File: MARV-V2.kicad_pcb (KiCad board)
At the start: 4 copper layers, 46.6 x 41.2 mm, 140 parts, among them J10 DBG pads (SWCLK SWDIO GND), J11 microSD, Molex 104031-0811 pu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, J3 ESC pads (CURR TX M4 M3 M2 M1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, J4 USB_C_PROGRAM_POWER, J6 IO array signal column (inner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, J7 IO array power column (5V / 3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, J8 IO array GND column (board ed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, SW1 RESET (RUN to GND), SW2 BOOTSEL (via R24), U12 TPS7A2033PDBVR, U20 RP2354B, U21 ICM-45686 6-axis IMU, U22 BMP581 barometer, U23 ADXL375 high-g accelerometer, U24 DNP: W25Q32JVSNIQ, 32 Mbit QS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, U25 TPS2121RUXR, U26 AP63205WU-7, U7 TPS62913RPUR, U8 USBLC6-2SC6, Y1 12 MHz TAXM12M4RFBCCT2T, CL 1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

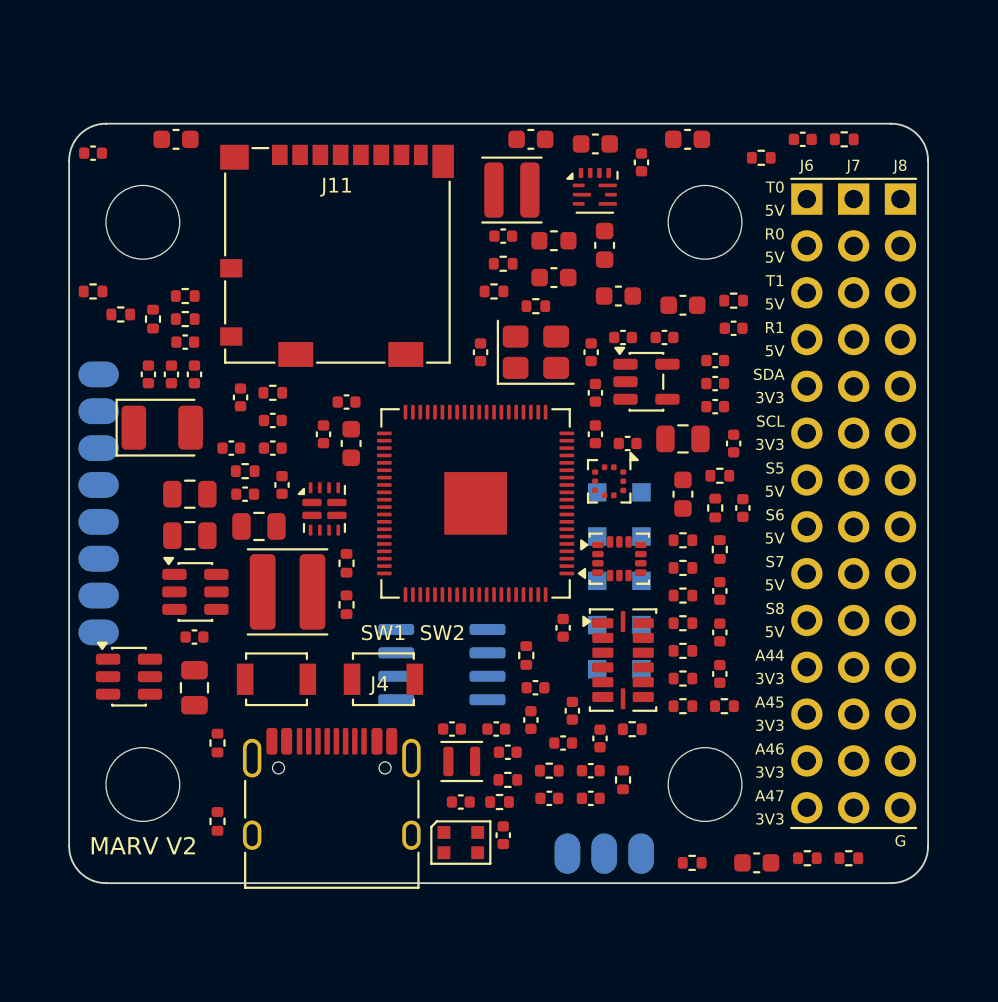
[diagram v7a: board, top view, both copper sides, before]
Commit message: Schematic re-organised into 11 per-subsystem pages, drawn as wired blocks
Each subsystem now has its own sheet (RP2354B, USB/debug, ICM-45686, BMP581,
ADXL375, microSD, QSPI expansion, VBAT buck + ESC row, priority mux, 3.3 V
rail, IO block) with the IC's own decoupling, pull-ups, test points and
connectors placed beside it and wired, labels only for nets leaving the
block. Root sheet is an index. tools/build_power.py grows a small layout
engine (wire routing, junctions, decoupling ladders, note flow) with
self-checks for dangling wires and multi-net wire islands; the long design
notes are preserved verbatim as module constants.

Purely presentational: netlist fingerprint (tools/netlist_fingerprint.py,
new) is identical before and after, ERC 0, power checks pass. PCB footprint
paths re-pointed at the new sheet UUIDs by tools/relink_pcb_paths.py (new);
the board diff is path lines only, DRC unconnected count unchanged.
README/DESIGN_SPEC sheet lists updated; pre-change sheets and generator in
backups/pre-sheet-reorg-2026-09-16/.

Also carries the uncommitted work that preceded it: PCB routing, plane
stitching and route-analysis tools (tools/route_*.py, stitch_planes.py),
GPIO remap in PINOUT.md / check_power_netlist.py / setup_pcb.py, and the
grommet mounting-hole footprint update.

Co-Authored-By: Claude Fable 5.1 <noreply@anthropic.com>
Claude-Session: https://claude.ai/code/session_01Y51PayhRcgfdi3hVsfn4qg
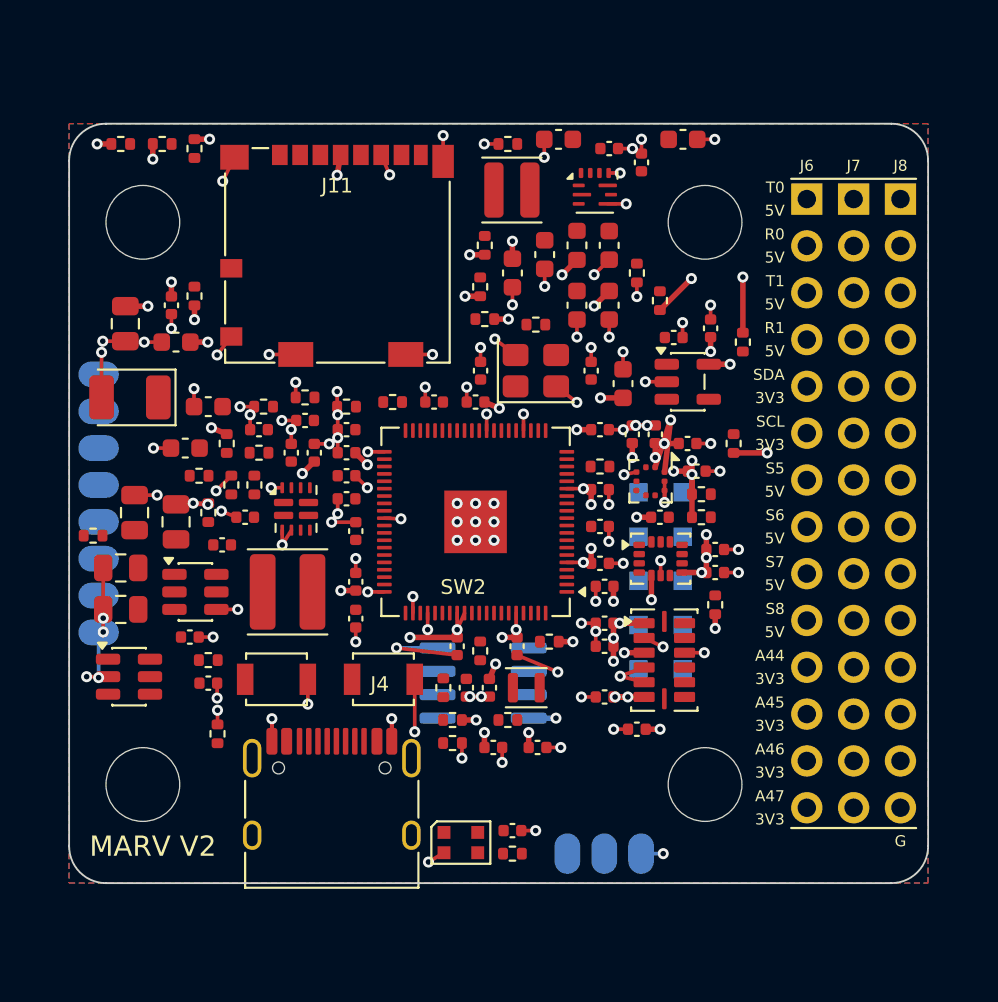
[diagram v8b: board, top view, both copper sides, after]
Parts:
- C48: value 100n / 16 V X7R, ADC0 -> 100n / 16 V X7R, ADC1
- C49: value 100n / 16 V X7R, ADC1 -> 100n / 16 V X7R, ADC0
- moved R40 39.4 mm to (81.8, 80.5)
- moved C21 38.7 mm to (84.2, 94.8), turned to 180 degrees
- moved R36 37.3 mm to (79.5, 80.5)
- moved R39 37.0 mm to (83.5, 80.8), turned to -90 degrees
- moved R54 35.0 mm to (94.2, 94.5)
- moved R41 33.7 mm to (83.5, 88.8), turned to 90 degrees
- moved R28 32.8 mm to (89.5, 94.2), turned to 180 degrees
- moved C66 30.9 mm to (79.8, 90.2), turned to -90 degrees
- moved R30 30.6 mm to (91.8, 94.8), turned to 180 degrees
- moved C65 28.7 mm to (82.5, 91.2), turned to 180 degrees
- moved C64 26.8 mm to (82.2, 89.2), turned to -90 degrees
- moved R4 25.3 mm to (84.8, 112.5), turned to 90 degrees
- moved R29 24.0 mm to (105.5, 98.0), turned to 180 degrees
- moved C45 23.7 mm to (87.0, 96.0), turned to 180 degrees
- moved R27 23.4 mm to (84.2, 108.5), turned to 0 degrees
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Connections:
- U20 pad 1: PWM3 -> HG_ACC_CS
- U20 pad 11: GPS_RX -> unconnected-(U20-GPIO12-Pad11)
- U20 pad 12: GPS_TX -> BARO_INT
- U20 pad 13: PWM7 -> BARO_CS
- U20 pad 14: PWM8 -> PWM7
- U20 pad 16: SENS_MISO -> ELRS_RX
- U20 pad 17: HG_ACC_CS -> ELRS_TX
- U20 pad 18: SENS_SCK -> unconnected-(U20-GPIO18-Pad18)
- U20 pad 19: SENS_MOSI -> PWM6
- U20 pad 2: PWM4 -> PWM8
- U20 pad 20: IMU_CS -> PWM5
- U20 pad 22: BARO_CS -> MAG_SDA
- U20 pad 23: IMU_INT1 -> MAG_SCL
- U20 pad 25: IMU_INT2 -> GPS_RX
- U20 pad 26: BARO_INT -> GPS_TX
- U20 pad 27: LED_DATA -> unconnected-(U20-GPIO26-Pad27)
- U20 pad 3: MAG_SDA -> IMU_INT1
- U20 pad 36: unconnected-(U20-GPIO28-Pad36) -> SD_D0
- U20 pad 37: HG_ACC_INT -> SD_D1
- U20 pad 38: ESC_TELEM_RX -> SD_D2
- U20 pad 39: unconnected-(U20-GPIO31-Pad39) -> SD_D3
- U20 pad 4: MAG_SCL -> IMU_CS
- U20 pad 40: SD_CLK -> ESC_TELEM_RX
- U20 pad 42: SD_CMD -> SD_CLK
- U20 pad 43: SD_D0 -> SD_CMD
- U20 pad 44: SD_D1 -> SD_DET
- U20 pad 45: SD_D2 -> PWM4
- U20 pad 46: SD_D3 -> PWR_SRC_ST
- U20 pad 47: SD_DET -> PWM3
- U20 pad 48: PWR_SRC_ST -> PWM2
- U20 pad 49: VBAT_SENSE -> VBUS_SENSE
- U20 pad 52: VBUS_SENSE -> VBAT_SENSE
- U20 pad 54: unconnected-(U20-GPIO43/ADC3-Pad54) -> PWM1
- U20 pad 6: ELRS_RX -> SENS_MISO
- U20 pad 7: ELRS_TX -> unconnected-(U20-GPIO9-Pad7)
- U20 pad 78: unconnected-(U20-GPIO1-Pad78) -> HG_ACC_INT
- U20 pad 79: PWM1 -> IMU_INT2
- U20 pad 8: PWM5 -> SENS_SCK
- U20 pad 80: PWM2 -> LED_DATA
- U20 pad 9: PWM6 -> SENS_MOSI
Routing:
- net GND: track 0.00 -> 113.4 mm, vias 0 -> 109
- net V3V3_SYS: track 0.00 -> 47.1 mm, vias 0 -> 44
- net V3V3_ANA: track 0.00 -> 28.3 mm, vias 0 -> 23
- added copper zone on B.Cu, net GND
- added copper zone on F.Cu, net GND
- added copper zone on In1.Cu, net GND
- added copper zone on In2.Cu, net V3V3_ANA
- added copper zone on In2.Cu, net V3V3_SYS
